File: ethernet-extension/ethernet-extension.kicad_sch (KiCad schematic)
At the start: 44 parts, among them J1 Wuerth_7499010121A, J2 East, J3 West, U1 W5500, Y1 25MHz

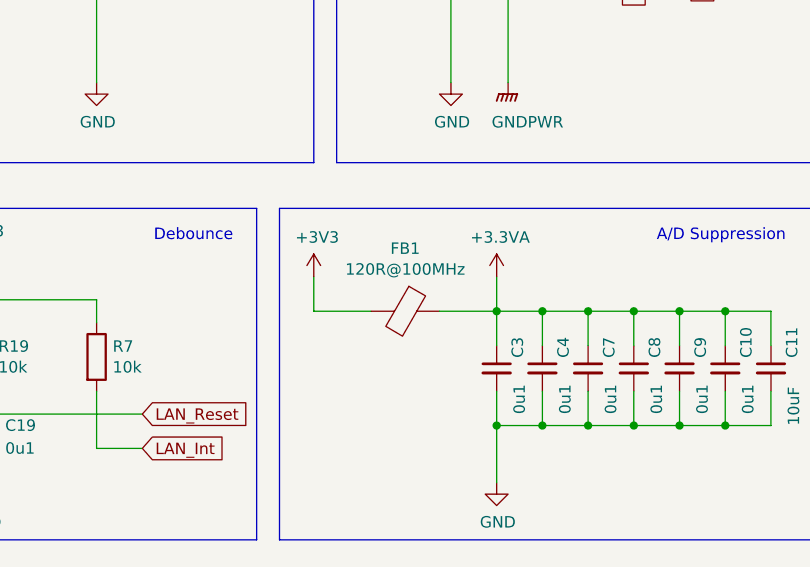
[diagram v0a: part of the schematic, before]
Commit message: Fixing more ERC errors
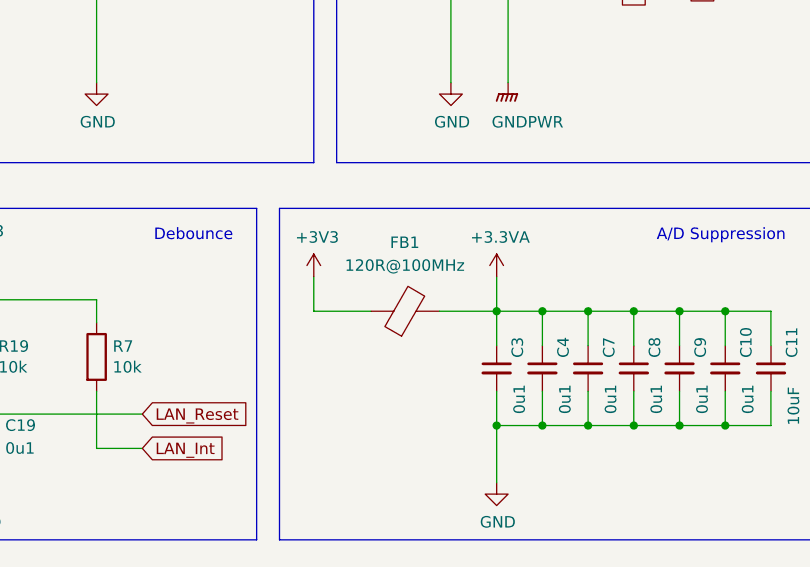
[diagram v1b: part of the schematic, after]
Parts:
- removed FB1: 120R@100MHz, Inductor_SMD:L_0805_2012Metric, symbol Device:Ferrite_Bead
- added FB1: 120R@100MHz, Inductor_SMD:L_0805_2012Metric, symbol Device:FerriteBead
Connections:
- net +3.3VA: now also FB1.2
- net +3V3: now also FB1.1
